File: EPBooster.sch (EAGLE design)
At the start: 33 parts, among them Q1 2N5457, Q2 2N5088, SW1 DIP 2 POS

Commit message: Changed files for v1.1
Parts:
- +9/18V: device gm-supply:+9V(T) -> mb_supply:+9V(T)
- C1, C7: device gm-caps-film-chicklet:075X0402 -> mb_caps-chicklet:075X0402
- C2, C3, C4, C6, C8, C9: device gm-caps-electro-pol:0631 -> mb_caps-electro:0631
- C5: device gm-caps-electro-pol:0631 -> mb_caps-electro:0801
- D1: device gm-diodes:1N4148-3 -> mb_diodes:1N4148-3
- G: device gm-supply:GND(T) -> mb_supply:GND(T)
- GAIN: device gm-pots:POT -> mb_pots:POT
- IN: device gm-supply:IN(T) -> mb_supply:IN(T)
- LED: device gm-supply:PAD -> mb_supply:PAD
- OUT: device gm-supply:OUT(T) -> mb_supply:OUT(T)
- Q1: device gm-trans:2N5457 -> mb_trans:2N5457
- Q2: device gm-trans:2N5088 -> mb_trans:2N5088
- R1, R10, R11, R12, R13, R14, R2, R3, R4, R5, R6, R7, R8, R9: device gm-resistors:6MM.3 -> mb_resistors:6MM.3
- SW1: device special:SW_DIP-2 -> mb_dip switch:SW_DIP-2

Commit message: New Board and Schematic for v1.2
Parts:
- C1, C7: device mb_caps-chicklet:075X0402 -> mb_caps-box:072X0252
- C2, C3, C4, C6, C8, C9: device mb_caps-electro:0631 -> mb_caps-electro:0501
- C5: device mb_caps-electro:0801 -> mb_caps-electro:0631
- LED: value 3mm -> 3MM; device mb_supply:PAD -> mb_diodes:LED3MM
- R1, R10, R11, R12, R13, R14, R2, R3, R4, R5, R6, R7, R8, R9: device mb_resistors:6MM.3 -> mb_resistors:3MM.2
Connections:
- net GND: now also LED.C
- net N$1: now also LED.A; no longer LED.PAD

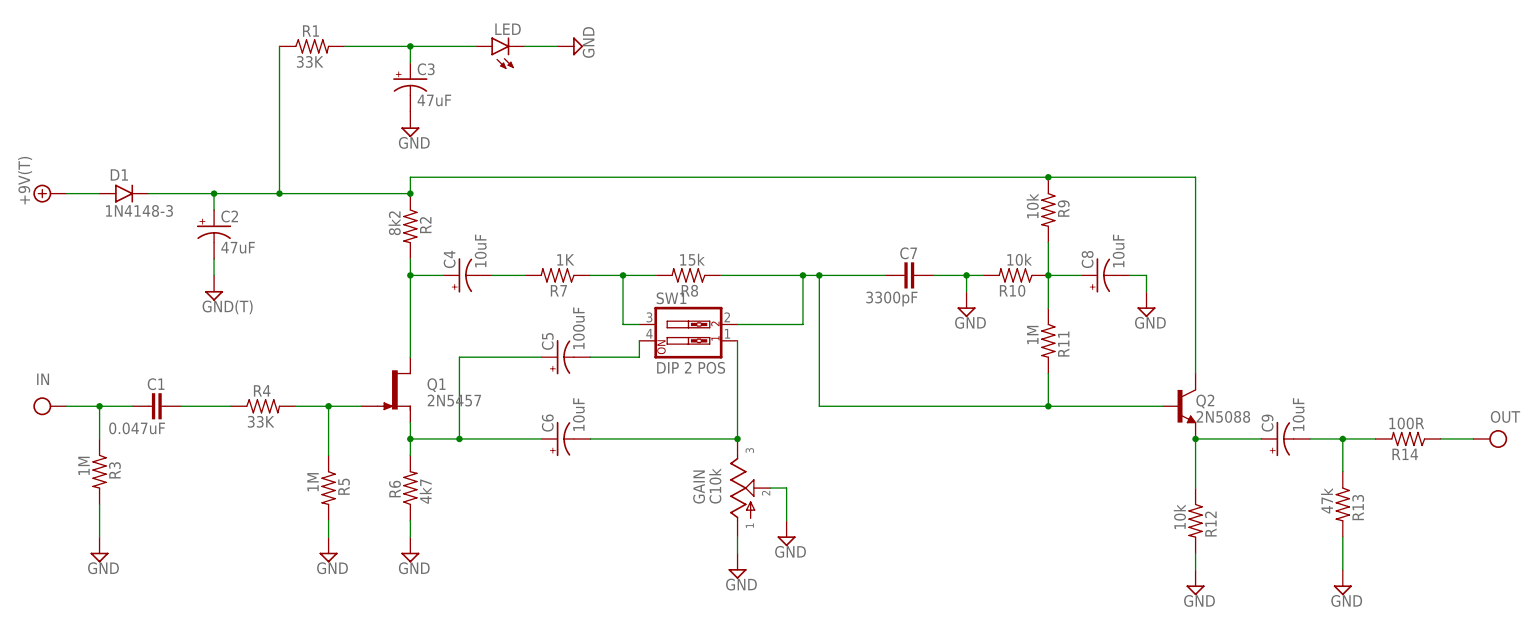
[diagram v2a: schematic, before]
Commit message: Changed board and schematic for v1.3
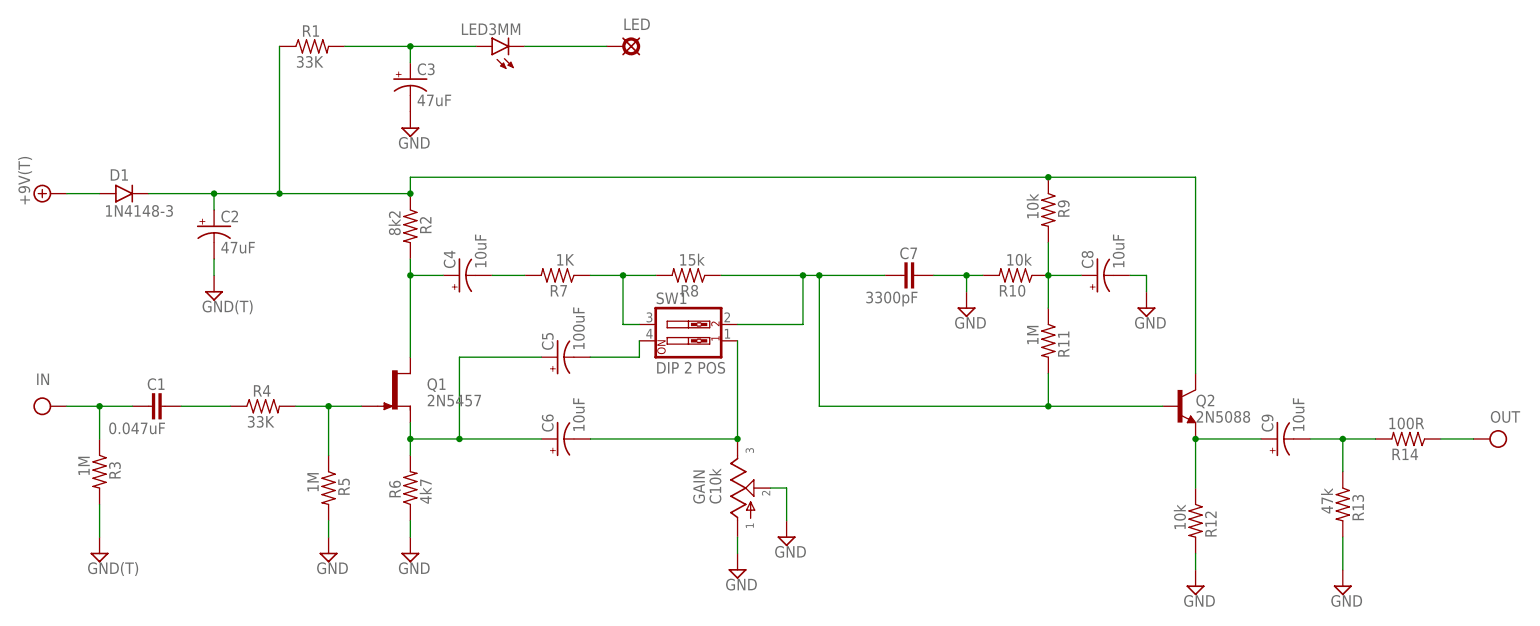
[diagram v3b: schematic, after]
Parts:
- added GND: GND(T), mb_supply:GND(T)
- added LED3MM: 3MM, mb_diodes:LED3MM
- LED: value 3MM -> (none); device mb_diodes:LED3MM -> mb_supply:PAD
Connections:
- new net N$14: LED.PAD, LED3MM.C
- net GND: now also GND.GND; no longer LED.C
- net N$1: now also LED3MM.A; no longer LED.A
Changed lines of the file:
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@@
 <parts>
 <part name="+9/18V" library="mb_supply" deviceset="+9V(T)" device=""/>
-<part name="G" library="mb_supply" deviceset="GND(T)" device=""/>
+<part name="GND" library="mb_supply" deviceset="GND(T)" device=""/>
 <part name="D1" library="mb_diodes" deviceset="1N4148" device="-3"/>
 <part name="C5" library="mb_caps-electro" deviceset="063" device="1" value="100uF"/>
@@
 <part name="C7" library="mb_caps-box" deviceset="072X025" device="2" value="3300pF"/>
 <part name="GND2" library="gm-supply" deviceset="GND" device=""/>
-<part name="GND3" library="gm-supply" deviceset="GND" device=""/>
 <part name="GND4" library="gm-supply" deviceset="GND" device=""/>
 <part name="GND5" library="gm-supply" deviceset="GND" device=""/>
@@
 <part name="C8" library="mb_caps-electro" deviceset="050" device="1" value="10uF"/>
 <part name="C9" library="mb_caps-electro" deviceset="050" device="1" value="10uF"/>
-<part name="LED" library="mb_diodes" deviceset="LED" device="3MM" value="3MM"/>
-<part name="GND1" library="gm-supply" deviceset="GND" device=""/>
+<part name="LED3MM" library="mb_diodes" deviceset="LED" device="3MM" value="3MM"/>
+<part name="LED" library="mb_supply" deviceset="PAD" device=""/>
+<part name="G" library="mb_supply" deviceset="GND(T)" device=""/>
 </parts>
 <sheets>
@@
 <instances>
 <instance part="+9/18V" gate="+9V" x="-5.08" y="76.2" rot="R90"/>
-<instance part="G" gate="GND" x="20.32" y="60.96"/>
+<instance part="GND" gate="GND" x="20.32" y="60.96"/>
 <instance part="D1" gate="G$1" x="7.62" y="76.2"/>
 <instance part="C5" gate="G$1" x="73.66" y="50.8" rot="R90"/>
@@
 <instance part="C7" gate="G$1" x="129.54" y="63.5" rot="R90"/>
 <instance part="GND2" gate="GND" x="50.8" y="86.36"/>
-<instance part="GND3" gate="GND" x="2.54" y="20.32"/>
 <instance part="GND4" gate="GND" x="137.16" y="58.42"/>
 <instance part="GND5" gate="GND" x="165.1" y="58.42"/>
@@
 <instance part="C8" gate="1" x="157.48" y="63.5" rot="R90"/>
 <instance part="C9" gate="1" x="185.42" y="38.1" rot="R90"/>
-<instance part="LED" gate="G$1" x="66.04" y="99.06" rot="R180"/>
-<instance part="GND1" gate="GND" x="76.2" y="99.06" rot="R90"/>
+<instance part="LED3MM" gate="G$1" x="66.04" y="99.06" rot="R180"/>
+<instance part="LED" gate="G$1" x="83.82" y="99.06"/>
+<instance part="G" gate="GND" x="2.54" y="20.32"/>
 </instances>
 <busses>
@@
 <wire x1="50.8" y1="96.52" x2="50.8" y2="99.06" width="0.1524" layer="91"/>
 <junction x="50.8" y="99.06"/>
-<pinref part="LED" gate="G$1" pin="A"/>
+<pinref part="LED3MM" gate="G$1" pin="A"/>
 </segment>
 </net>
 <net name="GND" class="0">
-<segment>
-<pinref part="GND3" gate="GND" pin="GND"/>
-<pinref part="R3" gate="G$1" pin="2"/>
-<wire x1="2.54" y1="22.86" x2="2.54" y2="27.94" width="0.1524" layer="91"/>
-</segment>
 <segment>
 <pinref part="GND8" gate="GND" pin="GND"/>
@@
 </segment>
 <segment>
-<pinref part="G" gate="GND" pin="GND"/>
+<pinref part="GND" gate="GND" pin="GND"/>
 <pinref part="C2" gate="1" pin="-"/>
 <wire x1="20.32" y1="63.5" x2="20.32" y2="66.04" width="0.1524" layer="91"/>
@@
 </segment>
 <segment>
-<pinref part="LED" gate="G$1" pin="C"/>
-<pinref part="GND1" gate="GND" pin="GND"/>
-<wire x1="68.58" y1="99.06" x2="73.66" y2="99.06" width="0.1524" layer="91"/>
+<pinref part="R3" gate="G$1" pin="2"/>
+<pinref part="G" gate="GND" pin="GND"/>
+<wire x1="2.54" y1="22.86" x2="2.54" y2="27.94" width="0.1524" layer="91"/>
 </segment>
 </net>
@@
 </segment>
 </net>
+<net name="N$14" class="0">
+<segment>
+<pinref part="LED" gate="G$1" pin="PAD"/>
+<pinref part="LED3MM" gate="G$1" pin="C"/>
+<wire x1="81.28" y1="99.06" x2="68.58" y2="99.06" width="0.1524" layer="91"/>
+</segment>
+</net>
